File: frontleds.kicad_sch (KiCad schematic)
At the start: 12 parts, among them IC2 STCS1APUR, IC3 STCS1APUR, J13 Conn_02x10_Odd_Even, J5 Conn_02x10_Odd_Even

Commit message: standardised components, removing mixed values
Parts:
- C19, C21: LCSC C1525 -> C307331
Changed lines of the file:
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@@
 			)
 		)
-		(property "LCSC" "C1525"
+		(property "LCSC" "C307331"
 			(at 123.19 71.12 0)
 			(effects
@@
 			)
 		)
-		(property "LCSC" "C1525"
+		(property "LCSC" "C307331"
 			(at 123.19 27.94 0)
 			(effects

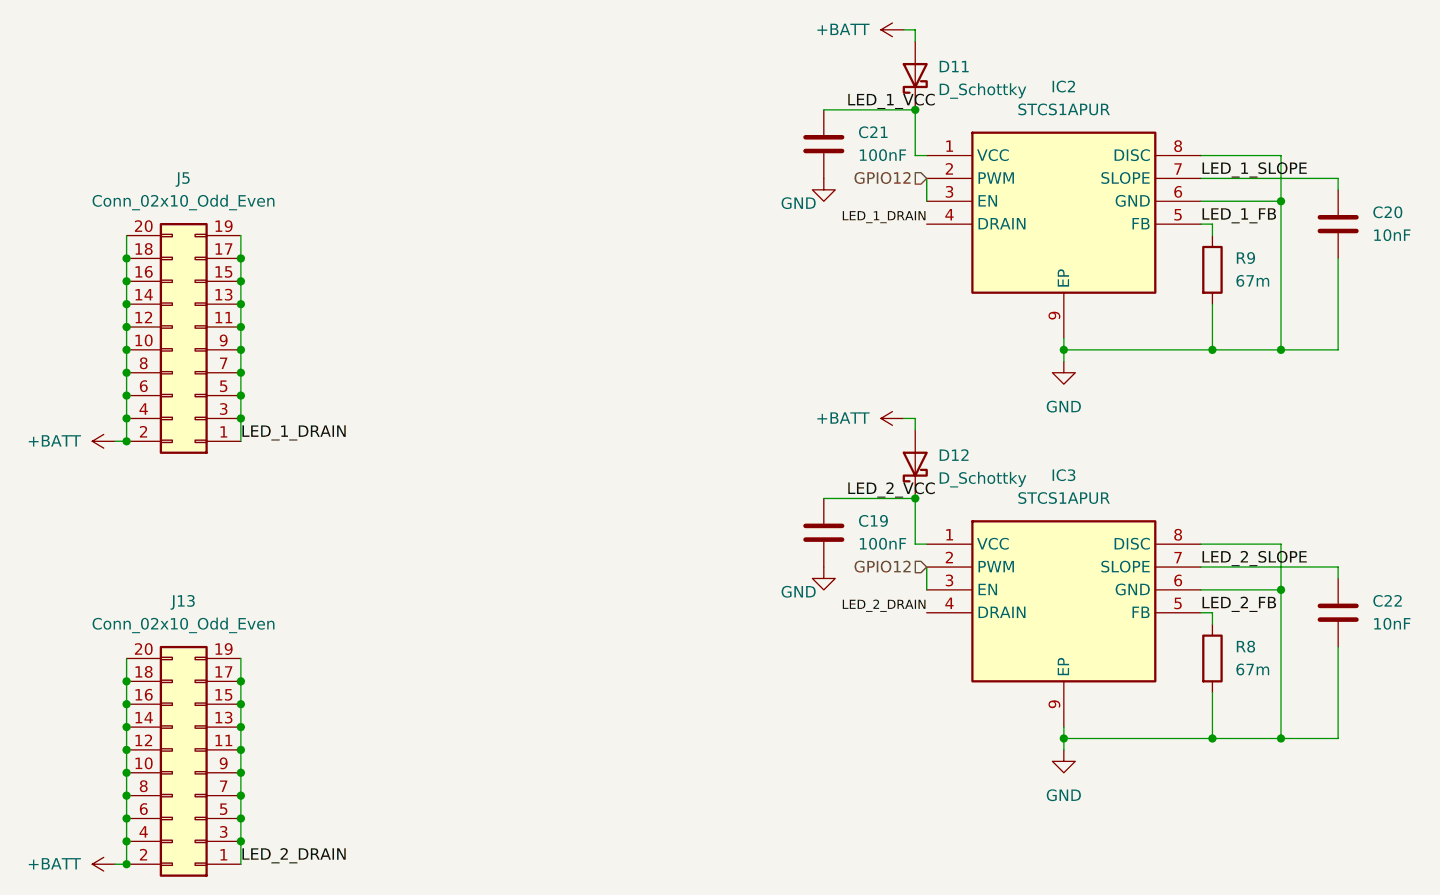
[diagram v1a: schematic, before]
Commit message: made front leds use 5v instead of batt for efficiency
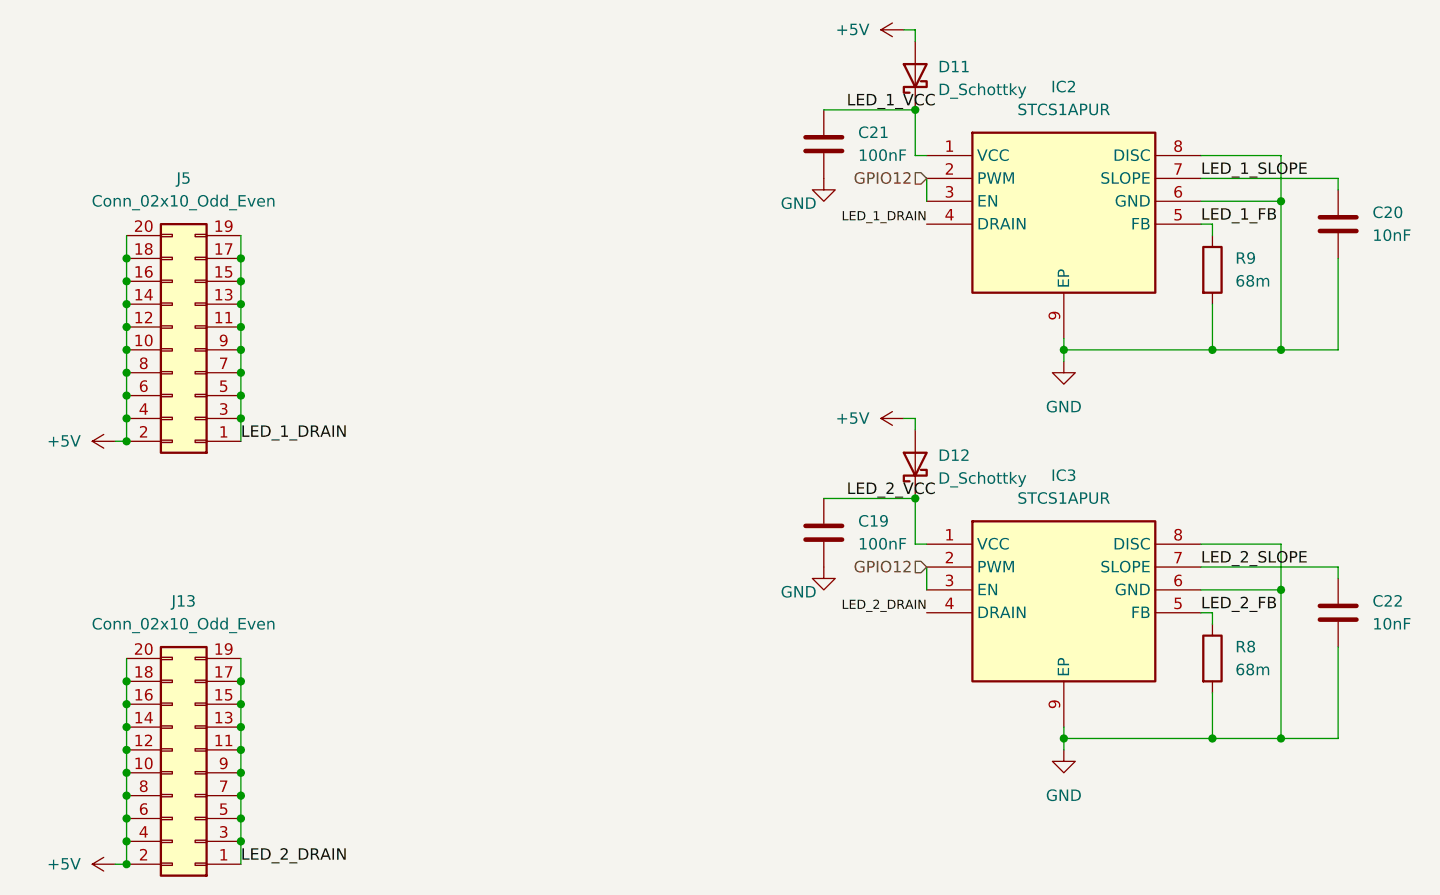
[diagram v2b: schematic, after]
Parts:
- R8, R9: value 67m -> 68m
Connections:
- net +BATT renamed +5V
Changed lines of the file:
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@@
-	)
-	(symbol
-		(lib_id "power:+BATT")
-		(at 132.08 15.24 90)
-		(unit 1)
-		(exclude_from_sim no)
-		(in_bom yes)
-		(on_board yes)
-		(dnp no)
-		(fields_autoplaced yes)
-		(property "Reference" "#PWR025"
-			(at 135.89 15.24 0)
-			(effects
-				(font
-					(size 1.27 1.27)
-				)
-				(hide yes)
-			)
-		)
-		(property "Value" "+BATT"
-			(at 128.27 15.2399 90)
-			(effects
-				(font
-					(size 1.27 1.27)
-				)
-				(justify left)
-			)
-		)
-		(property "Footprint" ""
-			(at 132.08 15.24 0)
-			(effects
-				(font
-					(size 1.27 1.27)
-				)
-				(hide yes)
-			)
-		)
-		(property "Datasheet" ""
-			(at 132.08 15.24 0)
-			(effects
-				(font
-					(size 1.27 1.27)
-				)
-				(hide yes)
-			)
-		)
-		(property "Description" "Power symbol creates a global label with name \"+BATT\""
-			(at 132.08 15.24 0)
-			(effects
-				(font
-					(size 1.27 1.27)
-				)
-				(hide yes)
-			)
-		)
-		(pin "1"
-		)
-		(instances
-			(project "robot_pcb"
-				(path "/2f56b371-1597-47e1-a48d-b7f69d342f77/f9fd353d-136c-4b1d-af31-404dc5242855"
-					(reference "#PWR025")
-					(unit 1)
-				)
-			)
-			(project "frontleds"
-				(path "/c5055a52-2a59-4ac7-8e13-bfa74af8a63f"
-					(reference "#PWR05")
-					(unit 1)
-				)
-			)
-		)
 	)
 	(symbol
@@
 	)
 	(symbol
-		(lib_id "power:+BATT")
+		(lib_id "power:+5V")
 		(at 44.45 107.95 90)
 		(unit 1)
@@
 			)
 		)
-		(property "Value" "+BATT"
+		(property "Value" "+5V"
 			(at 40.64 107.9499 90)
 			(effects
@@
 			)
 		)
-		(property "Description" "Power symbol creates a global label with name \"+BATT\""
+		(property "Description" "Power symbol creates a global label with name \"+5V\""
 			(at 44.45 107.95 0)
 			(effects
@@
 		)
 		(instances
-			(project "robot_pcb"
+			(project ""
 				(path "/2f56b371-1597-47e1-a48d-b7f69d342f77/f9fd353d-136c-4b1d-af31-404dc5242855"
 					(reference "#PWR027")
-					(unit 1)
-				)
-			)
-			(project "frontleds"
-				(path "/c5055a52-2a59-4ac7-8e13-bfa74af8a63f"
-					(reference "#PWR02")
 					(unit 1)
 				)
@@
 			)
 		)
-		(property "Value" "67m"
+		(property "Value" "68m"
 			(at 168.91 43.1799 0)
 			(effects
@@
 	)
 	(symbol
+		(lib_id "power:+5V")
+		(at 132.08 15.24 90)
+		(unit 1)
+		(exclude_from_sim no)
+		(in_bom yes)
+		(on_board yes)
+		(dnp no)
+		(fields_autoplaced yes)
+		(property "Reference" "#PWR025"
+			(at 135.89 15.24 0)
+			(effects
+				(font
+					(size 1.27 1.27)
+				)
+				(hide yes)
+			)
+		)
+		(property "Value" "+5V"
+			(at 128.27 15.2399 90)
+			(effects
+				(font
+					(size 1.27 1.27)
+				)
+				(justify left)
+			)
+		)
+		(property "Footprint" ""
+			(at 132.08 15.24 0)
+			(effects
+				(font
+					(size 1.27 1.27)
+				)
+				(hide yes)
+			)
+		)
+		(property "Datasheet" ""
+			(at 132.08 15.24 0)
+			(effects
+				(font
+					(size 1.27 1.27)
+				)
+				(hide yes)
+			)
+		)
+		(property "Description" "Power symbol creates a global label with name \"+5V\""
+			(at 132.08 15.24 0)
+			(effects
+				(font
+					(size 1.27 1.27)
+				)
+				(hide yes)
+			)
+		)
+		(pin "1"
+		)
+		(instances
+			(project "robot_pcb"
+				(path "/2f56b371-1597-47e1-a48d-b7f69d342f77/f9fd353d-136c-4b1d-af31-404dc5242855"
+					(reference "#PWR025")
+					(unit 1)
+				)
+			)
+		)
+	)
+	(symbol
 		(lib_id "Connector_Generic:Conn_02x10_Odd_Even")
 		(at 53.34 97.79 180)
@@
 	)
 	(symbol
-		(lib_id "power:+BATT")
+		(lib_id "power:+5V")
 		(at 132.08 58.42 90)
 		(unit 1)
@@
 			)
 		)
-		(property "Value" "+BATT"
+		(property "Value" "+5V"
 			(at 128.27 58.4199 90)
 			(effects
@@
 			)
 		)
-		(property "Description" "Power symbol creates a global label with name \"+BATT\""
+		(property "Description" "Power symbol creates a global label with name \"+5V\""
 			(at 132.08 58.42 0)
 			(effects
@@
 				)
 			)
-			(project "frontleds"
-				(path "/c5055a52-2a59-4ac7-8e13-bfa74af8a63f"
-					(reference "#PWR06")
-					(unit 1)
-				)
-			)
-		)
-	)
-	(symbol
-		(lib_id "power:+BATT")
+		)
+	)
+	(symbol
+		(lib_id "power:+5V")
 		(at 44.45 60.96 90)
 		(unit 1)
@@
 			)
 		)
-		(property "Value" "+BATT"
+		(property "Value" "+5V"
 			(at 40.64 60.9599 90)
 			(effects
@@
 			)
 		)
-		(property "Description" "Power symbol creates a global label with name \"+BATT\""
+		(property "Description" "Power symbol creates a global label with name \"+5V\""
 			(at 44.45 60.96 0)
 			(effects
@@
 		)
 		(instances
-			(project "robot_pcb"
+			(project ""
 				(path "/2f56b371-1597-47e1-a48d-b7f69d342f77/f9fd353d-136c-4b1d-af31-404dc5242855"
 					(reference "#PWR020")
-					(unit 1)
-				)
-			)
-			(project "frontleds"
-				(path "/c5055a52-2a59-4ac7-8e13-bfa74af8a63f"
-					(reference "#PWR01")
 					(unit 1)
 				)
@@
 			)
 		)
-		(property "Value" "67m"
+		(property "Value" "68m"
 			(at 168.91 86.3599 0)
 			(effects

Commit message: lcsc for 68m resistors
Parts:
- R8, R9: LCSC (none) -> C728416
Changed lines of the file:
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@@
+			)
+		)
+		(property "LCSC" "C728416"
+			(at 166.37 41.91 0)
+			(effects
+				(font
+					(size 1.27 1.27)
+				)
+				(hide yes)
 			)
 		)
@@
 			(at 166.37 85.09 0)
 			(effects
+				(font
+					(size 1.27 1.27)
+				)
+				(hide yes)
+			)
+		)
+		(property "LCSC" "C728416"
+			(at 166.37 85.09 0)
+			(effects

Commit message: another diode
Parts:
- D11, D12: LCSC (none) -> C83528
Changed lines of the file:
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@@
+			)
+		)
+		(property "LCSC" "C83528"
+			(at 133.35 63.5 90)
+			(effects
+				(font
+					(size 1.27 1.27)
+				)
+				(hide yes)
 			)
 		)
@@
 			(effects
 				(font
+					(size 1.27 1.27)
+				)
+				(hide yes)
+			)
+		)
+		(property "LCSC" "C83528"
+			(at 133.35 20.32 90)
+			(effects
+				(font
